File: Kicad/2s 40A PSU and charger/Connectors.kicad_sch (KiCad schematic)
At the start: 18 parts, among them J1 Keystone 3579, J10 G-Switch-GT-USB-7025, J11 1.27mm 4 pin socket, J2 JST XH-S Balance Plug, J3 Keystone 3579, J4 Keystone 3569, J5 Keystone 3569, J6 Keystone 3579, J7 Keystone 3579, J8 Keystone 3569, J9 Keystone 3569

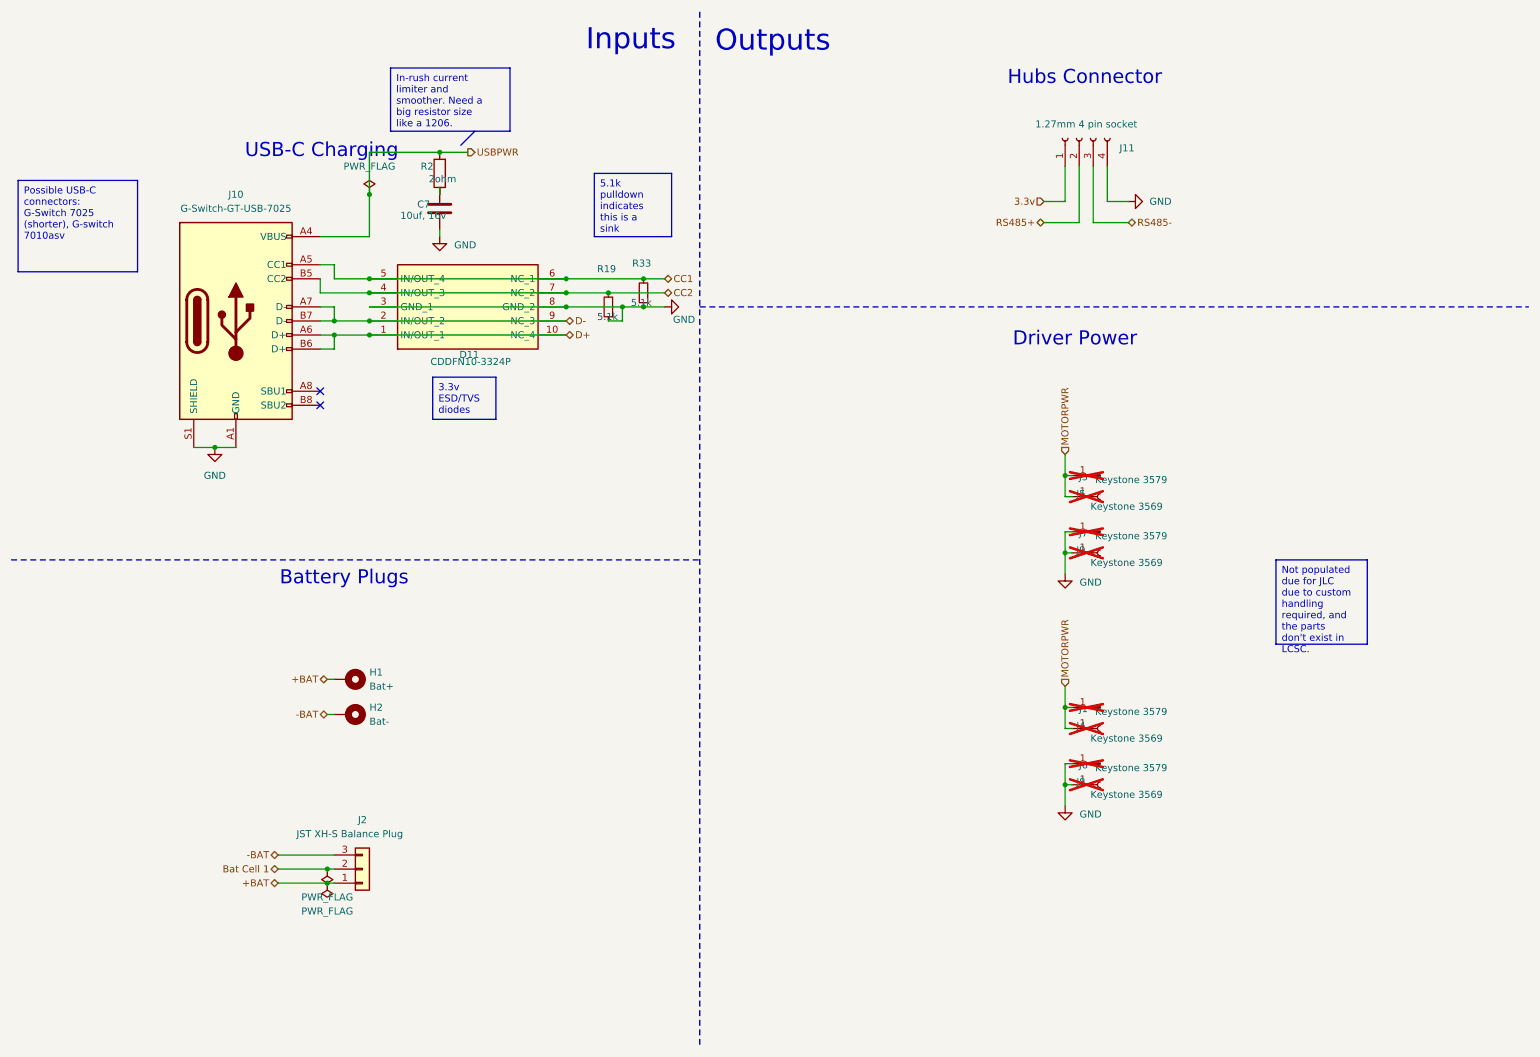
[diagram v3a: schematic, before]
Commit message: Added LCSC part numbers, DNP attr, and exported Gerbers
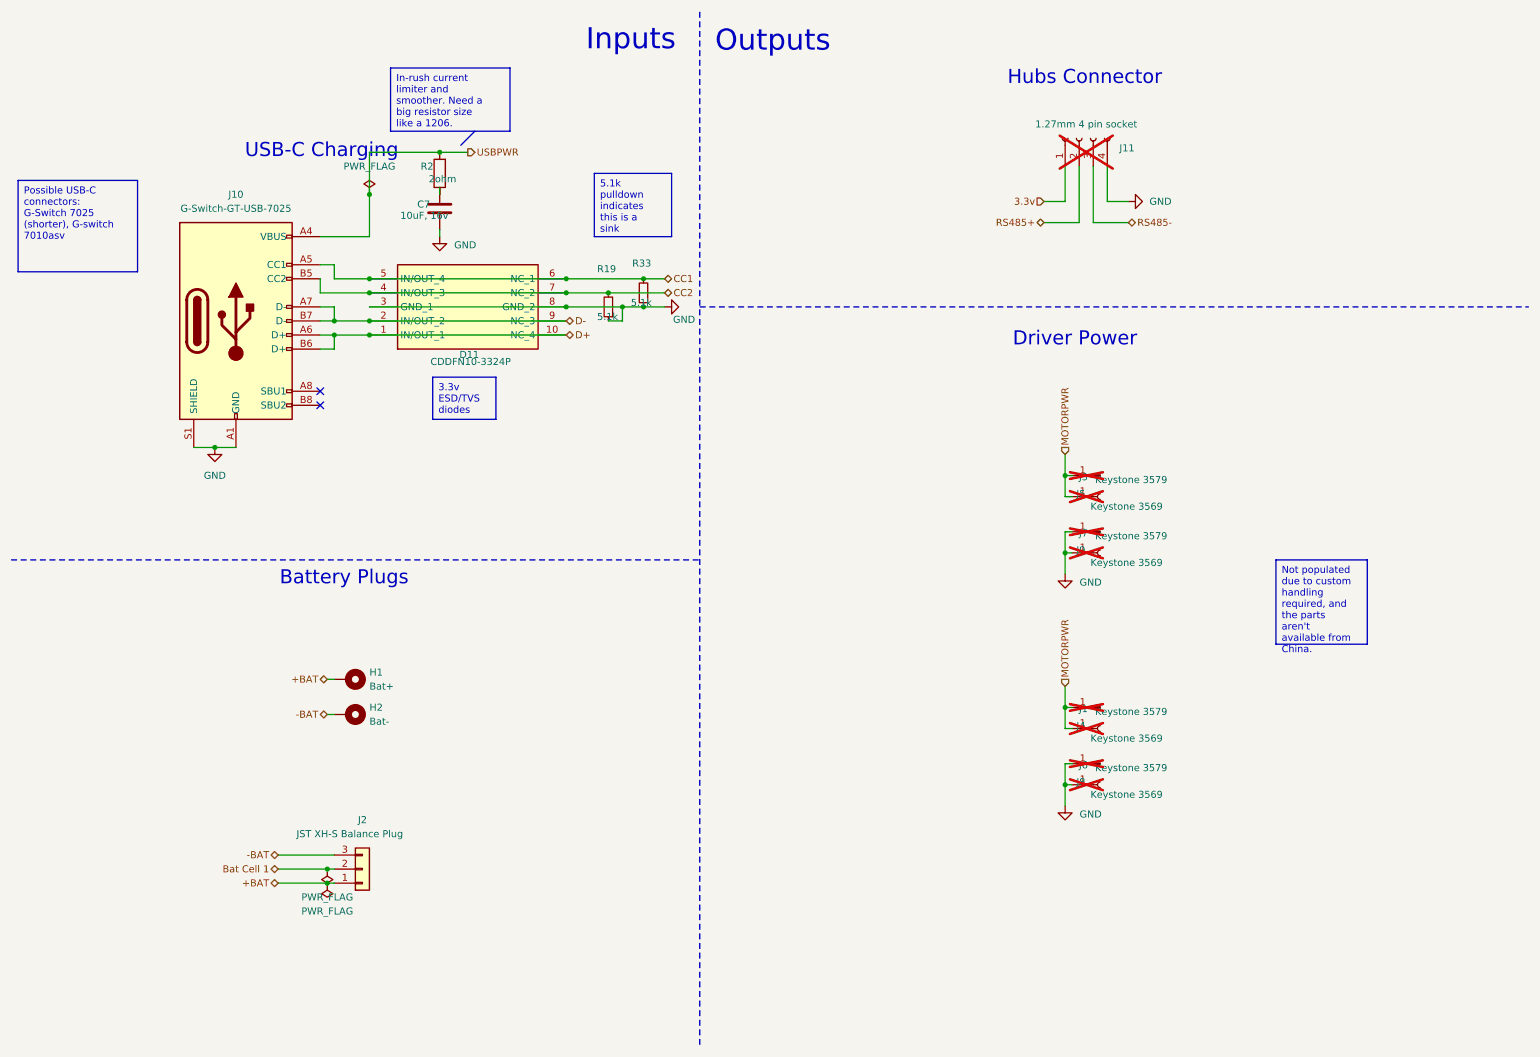
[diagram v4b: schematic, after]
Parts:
- C7: value 10uf, 16v -> 10uF, 16v; LCSC (none) -> C15850
- D11: LCSC (none) -> C913227
- J10: LCSC (none) -> C963213
- J11: now not fitted
- J2: LCSC (none) -> C161860
- R19, R33: LCSC (none) -> C25905
- R2: LCSC (none) -> C17521
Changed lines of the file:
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@@
 		)
 	)
-	(text_box "Not populated due for JLC due to custom handling required, and the parts don't exist in LCSC."
+	(text_box "Not populated due to custom handling required, and the parts aren't available from China."
 		(exclude_from_sim no)
 		(at 240.03 110.49 0)
@@
 			)
 		)
+		(property "LCSC" "C17521"
+			(at 86.614 39.37 0)
+			(effects
+				(font
+					(size 1.27 1.27)
+				)
+				(hide yes)
+			)
+		)
 		(pin "2"
 		)
@@
 			)
 		)
-		(property "Value" "10uf, 16v"
+		(property "Value" "10uF, 16v"
 			(at 81.788 48.26 0)
 			(effects
@@
 		(property "Description" "Unpolarized capacitor"
 			(at 88.9 46.99 0)
+			(effects
+				(font
+					(size 1.27 1.27)
+				)
+				(hide yes)
+			)
+		)
+		(property "LCSC" "C15850"
+			(at 84.836 46.228 0)
 			(effects
 				(font
@@
 			)
 		)
+		(property "LCSC" "C25905"
+			(at 117.348 57.912 0)
+			(effects
+				(font
+					(size 1.27 1.27)
+				)
+				(hide yes)
+			)
+		)
 		(pin "1"
 		)
@@
 			)
 		)
+		(property "LCSC" "C161860"
+			(at 74.93 166.37 0)
+			(effects
+				(font
+					(size 1.27 1.27)
+				)
+				(hide yes)
+			)
+		)
 		(pin "2"
 		)
@@
 				)
 				(justify left top)
+				(hide yes)
+			)
+		)
+		(property "LCSC" "C913227"
+			(at 94.234 73.406 0)
+			(effects
+				(font
+					(size 1.27 1.27)
+				)
 				(hide yes)
 			)
@@
 			)
 		)
+		(property "LCSC" "C963213"
+			(at 52.07 44.45 0)
+			(effects
+				(font
+					(size 1.27 1.27)
+				)
+				(hide yes)
+			)
+		)
 		(pin "B4"
 		)
@@
 		(property "Description" "Resistor, small symbol"
 			(at 125.73 62.23 0)
+			(effects
+				(font
+					(size 1.27 1.27)
+				)
+				(hide yes)
+			)
+		)
+		(property "LCSC" "C25905"
+			(at 123.698 56.896 0)
 			(effects
 				(font
@@
 		(in_bom yes)
 		(on_board yes)
-		(dnp no)
+		(dnp yes)
 		(property "Reference" "J11"
 			(at 213.106 36.068 90)
